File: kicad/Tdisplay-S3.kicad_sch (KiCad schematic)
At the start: 24 parts, among them J2 Conn_01x04, M1 Fan_4pin, M2 Fan_4pin, U11 T-Display-S3, U12 EMC2302-1, U13 TMP1075NDRLR, U14 TMP1075NDRLR

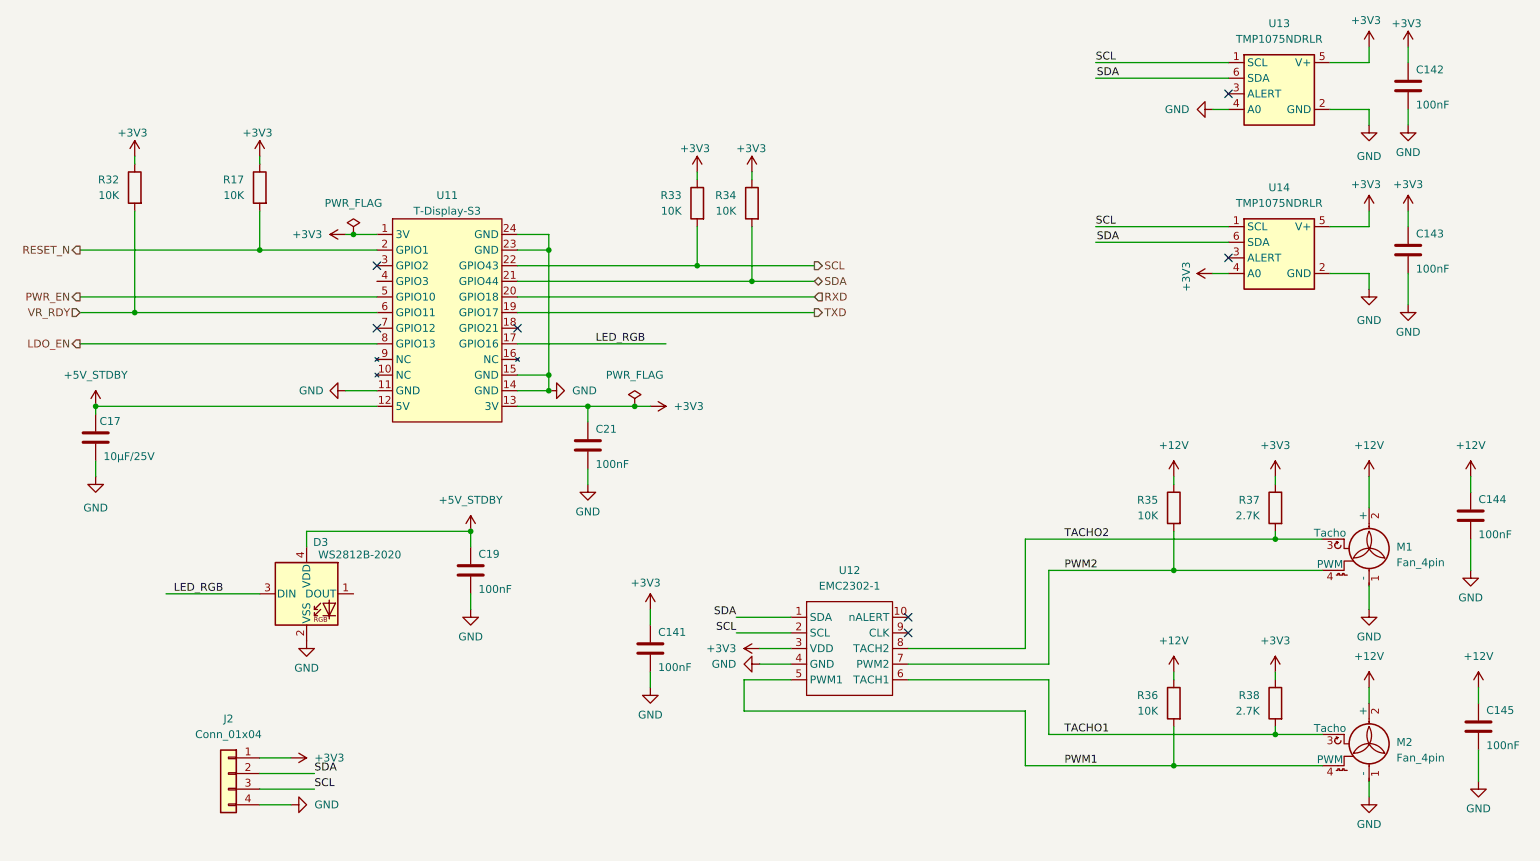
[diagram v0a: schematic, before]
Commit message: final update
Version 1.0 : working as expected, 14TH/s
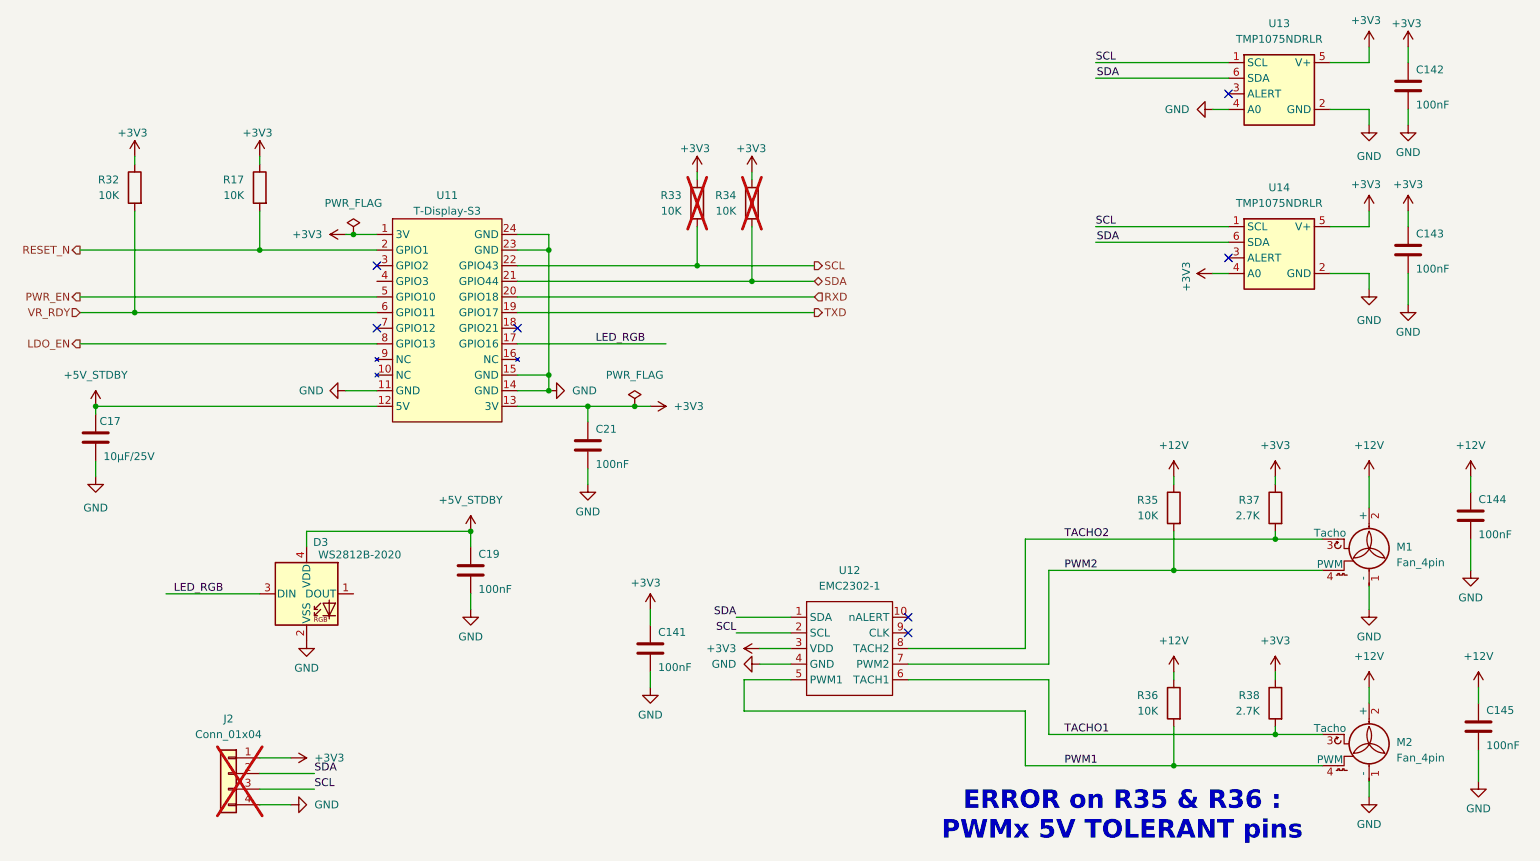
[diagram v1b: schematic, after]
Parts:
- C141, C142, C143, C144, C145, C19, C21: P/N LCSC (none) -> C476766
- C17: P/N LCSC (none) -> C6119887
- D3: P/N LCSC (none) -> C965555
- J2: now not fitted
- M1, M2: P/N LCSC (none) -> C240840
- R17, R32, R35, R36: P/N LCSC (none) -> C84376
- R33, R34: P/N LCSC (none) -> C84376; now not fitted
- R37, R38: P/N LCSC (none) -> C2907236
- U12: P/N LCSC (none) -> C626969
- U13, U14: P/N LCSC (none) -> C3663690
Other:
- note added: "ERROR on R35 & R36 : PWMx 5V TOLERANT pins"
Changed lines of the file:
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@@
 		)
 	)
+	(text "ERROR on R35 & R36 : \nPWMx 5V TOLERANT pins"
+		(exclude_from_sim no)
+		(at 196.088 150.368 0)
+		(effects
+			(font
+				(size 3 3)
+				(thickness 0.6)
+				(bold yes)
+				(color 255 0 0 1)
+			)
+		)
+	)
 	(label "SDA"
 		(at 64.77 143.51 0)
@@
 			)
 		)
+		(property "P/N LCSC" "C476766"
+			(at 242.57 58.42 0)
+			(effects
+				(font
+					(size 1.27 1.27)
+				)
+				(hide yes)
+			)
+		)
 		(pin "1"
 		)
@@
 			)
 		)
+		(property "P/N LCSC" "C240840"
+			(at 236.22 107.95 0)
+			(effects
+				(font
+					(size 1.27 1.27)
+				)
+				(hide yes)
+			)
+		)
 		(pin "1"
 		)
@@
 			)
 		)
+		(property "P/N LCSC" "C84376"
+			(at 204.47 132.08 0)
+			(effects
+				(font
+					(size 1.27 1.27)
+				)
+				(hide yes)
+			)
+		)
 		(pin "1"
 		)
@@
 			)
 		)
+		(property "P/N LCSC" "C476766"
+			(at 242.57 31.75 0)
+			(effects
+				(font
+					(size 1.27 1.27)
+				)
+				(hide yes)
+			)
+		)
 		(pin "1"
 		)
@@
 			)
 		)
+		(property "P/N LCSC" "C476766"
+			(at 252.73 101.6 0)
+			(effects
+				(font
+					(size 1.27 1.27)
+				)
+				(hide yes)
+			)
+		)
 		(pin "1"
 		)
@@
 			)
 		)
+		(property "P/N LCSC" "C2907236"
+			(at 220.98 132.08 0)
+			(effects
+				(font
+					(size 1.27 1.27)
+				)
+				(hide yes)
+			)
+		)
 		(pin "1"
 		)
@@
 			)
 		)
+		(property "P/N LCSC" "C476766"
+			(at 109.22 90.17 0)
+			(effects
+				(font
+					(size 1.27 1.27)
+				)
+				(hide yes)
+			)
+		)
 		(pin "1"
 		)
@@
 		(in_bom yes)
 		(on_board yes)
-		(dnp no)
+		(dnp yes)
 		(property "Reference" "R33"
 			(at 124.46 49.53 0)
@@
 			)
 		)
+		(property "P/N LCSC" "C84376"
+			(at 127 50.8 0)
+			(effects
+				(font
+					(size 1.27 1.27)
+				)
+				(hide yes)
+			)
+		)
 		(pin "1"
 		)
@@
 			)
 		)
+		(property "P/N LCSC" "C626969"
+			(at 153.67 128.27 0)
+			(effects
+				(font
+					(size 1.27 1.27)
+				)
+				(hide yes)
+			)
+		)
 		(pin "10"
 		)
@@
 		(in_bom yes)
 		(on_board yes)
-		(dnp no)
+		(dnp yes)
 		(fields_autoplaced yes)
 		(property "Reference" "J2"
@@
 			)
 		)
+		(property "P/N LCSC" "C3663690"
+			(at 213.36 26.67 0)
+			(effects
+				(font
+					(size 1.27 1.27)
+				)
+				(hide yes)
+			)
+		)
 		(pin "6"
 		)
@@
 			)
 		)
+		(property "P/N LCSC" "C84376"
+			(at 35.56 48.26 0)
+			(effects
+				(font
+					(size 1.27 1.27)
+				)
+				(hide yes)
+			)
+		)
 		(pin "1"
 		)
@@
 			)
 		)
+		(property "P/N LCSC" "C84376"
+			(at 204.47 100.33 0)
+			(effects
+				(font
+					(size 1.27 1.27)
+				)
+				(hide yes)
+			)
+		)
 		(pin "1"
 		)
@@
 			)
 		)
+		(property "P/N LCSC" "C240840"
+			(at 236.22 139.7 0)
+			(effects
+				(font
+					(size 1.27 1.27)
+				)
+				(hide yes)
+			)
+		)
 		(pin "1"
 		)
@@
 			)
 		)
+		(property "P/N LCSC" "C476766"
+			(at 119.38 123.19 0)
+			(effects
+				(font
+					(size 1.27 1.27)
+				)
+				(hide yes)
+			)
+		)
 		(pin "1"
 		)
@@
 			)
 		)
+		(property "P/N LCSC" "C3663690"
+			(at 213.36 53.34 0)
+			(effects
+				(font
+					(size 1.27 1.27)
+				)
+				(hide yes)
+			)
+		)
 		(pin "6"
 		)
@@
 		(in_bom yes)
 		(on_board yes)
-		(dnp no)
+		(dnp yes)
 		(property "Reference" "R34"
 			(at 133.35 49.53 0)
@@
 			)
 		)
+		(property "P/N LCSC" "C84376"
+			(at 135.89 50.8 0)
+			(effects
+				(font
+					(size 1.27 1.27)
+				)
+				(hide yes)
+			)
+		)
 		(pin "1"
 		)
@@
 			)
 		)
+		(property "P/N LCSC" "C84376"
+			(at 55.88 48.26 0)
+			(effects
+				(font
+					(size 1.27 1.27)
+				)
+				(hide yes)
+			)
+		)
 		(pin "1"
 		)
@@
 			)
 		)
+		(property "P/N LCSC" "C476766"
+			(at 90.17 110.49 0)
+			(effects
+				(font
+					(size 1.27 1.27)
+				)
+				(hide yes)
+			)
+		)
 		(pin "1"
 		)
@@
 			)
 		)
+		(property "P/N LCSC" "C965555"
+			(at 63.5 114.3 0)
+			(effects
+				(font
+					(size 1.27 1.27)
+				)
+				(hide yes)
+			)
+		)
 		(pin "2"
 		)
@@
 			)
 		)
+		(property "P/N LCSC" "C2907236"
+			(at 220.98 100.33 0)
+			(effects
+				(font
+					(size 1.27 1.27)
+				)
+				(hide yes)
+			)
+		)
 		(pin "1"
 		)
@@
 			)
 		)
+		(property "P/N LCSC" "C476766"
+			(at 254 135.89 0)
+			(effects
+				(font
+					(size 1.27 1.27)
+				)
+				(hide yes)
+			)
+		)
 		(pin "1"
 		)
@@
 			(at 29.21 88.9 0)
 			(effects
+				(font
+					(size 1.27 1.27)
+				)
+				(hide yes)
+			)
+		)
+		(property "P/N LCSC" "C6119887"
+			(at 29.21 88.9 0)
+			(effects
